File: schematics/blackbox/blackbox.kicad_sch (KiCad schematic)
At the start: 48 parts, among them J101 Micro_SD_Card, J102 Micro_SD_Card, J103 SWD, J104 F_COMPUTER, U101 STM32F405RGT6, U102 MAX14787E, Y101 26M

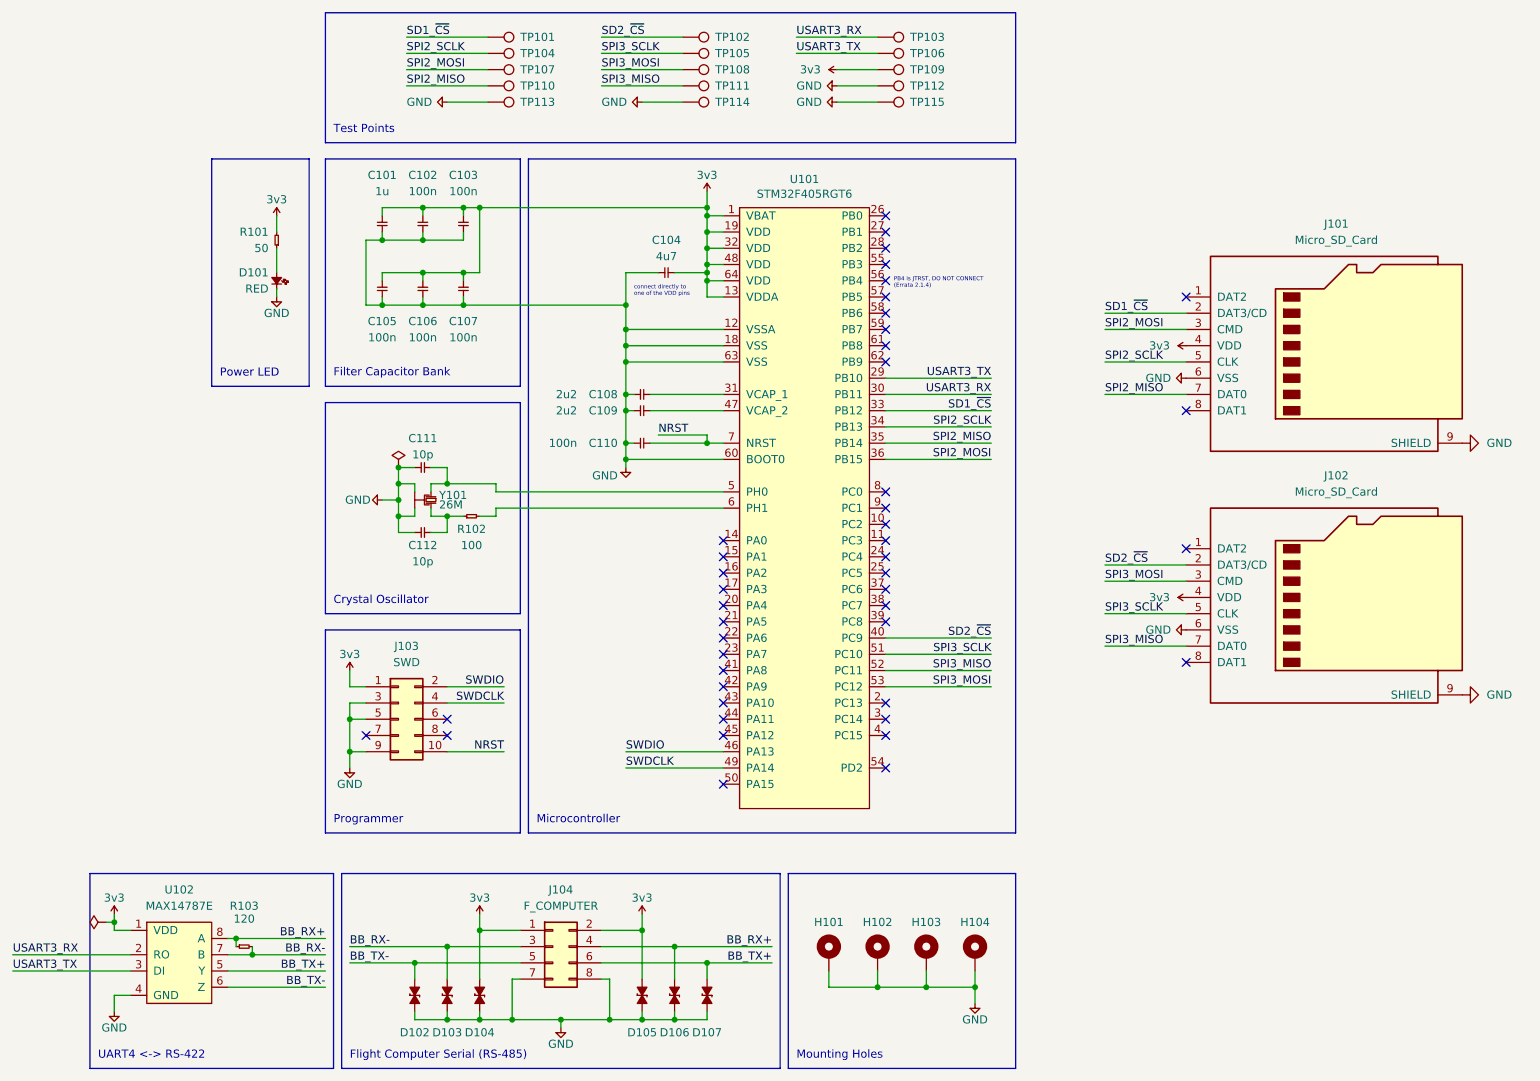
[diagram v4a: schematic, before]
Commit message: Minor changes to pass ERC
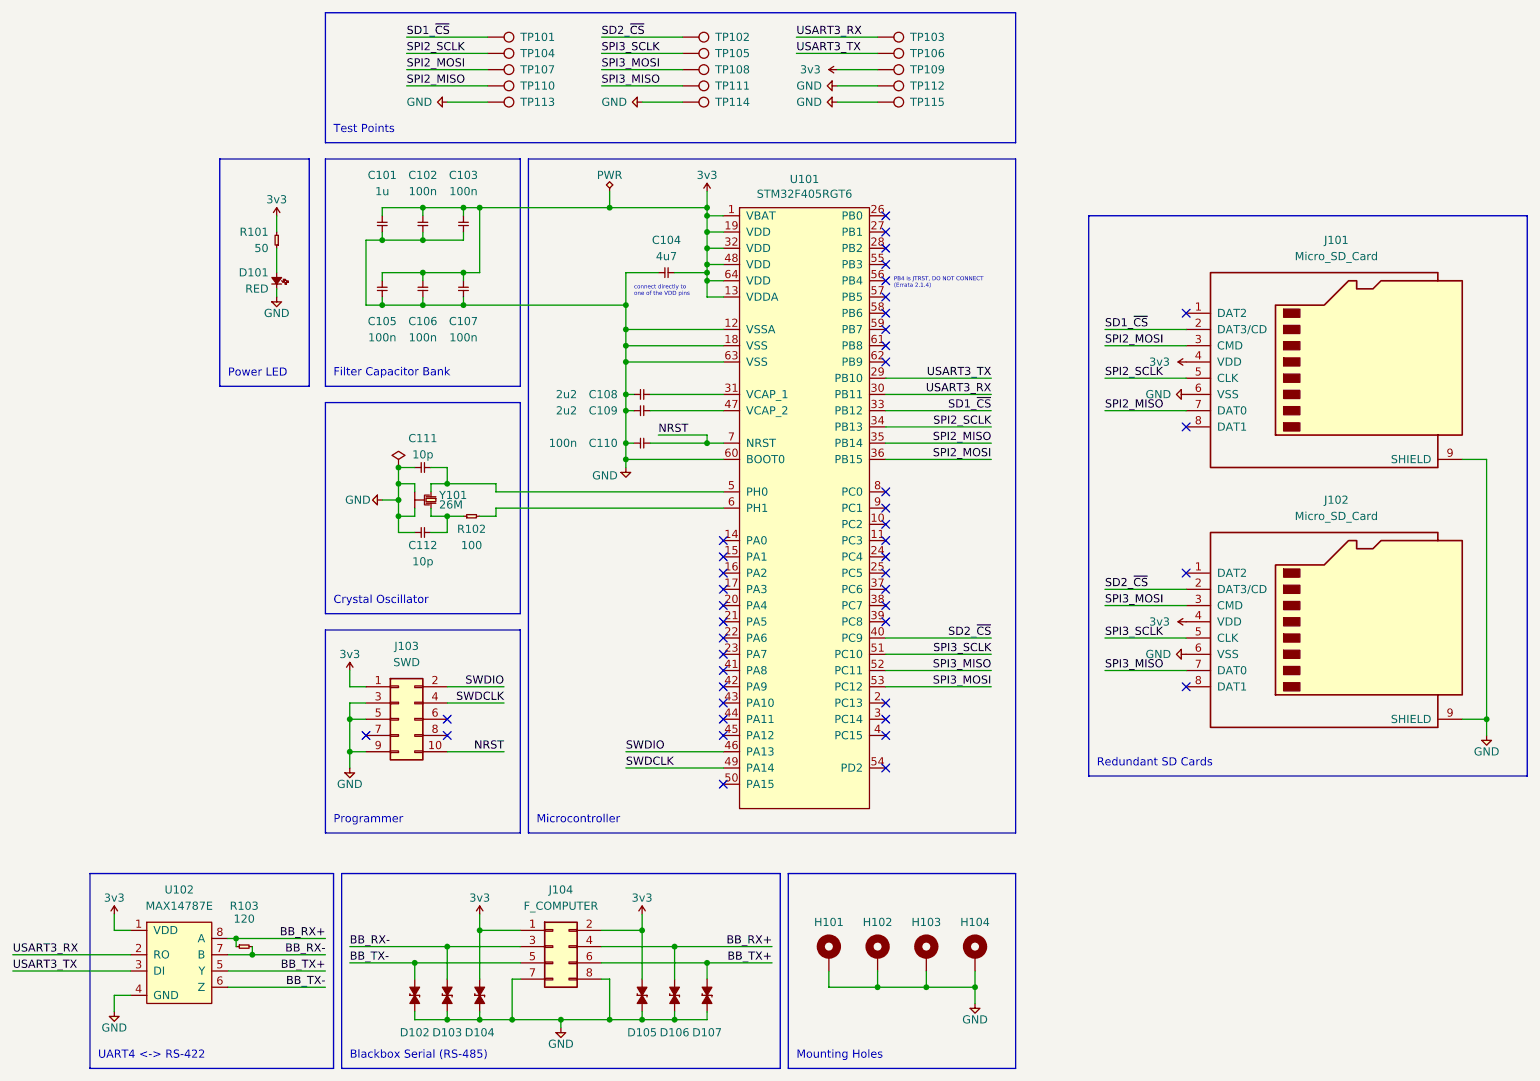
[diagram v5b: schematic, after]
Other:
- note added: "Blackbox Serial (RS-485)"
- note added: "Redundant SD Cards"
- note removed: "Flight Computer Serial (RS-485)"
- moved on the sheet: J101, J102
